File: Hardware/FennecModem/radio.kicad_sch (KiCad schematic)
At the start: 12 parts, among them J201 Conn_Coaxial, U201 DRA818V

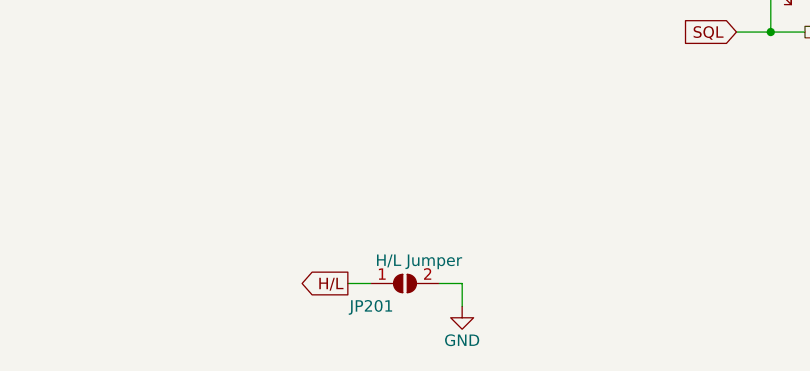
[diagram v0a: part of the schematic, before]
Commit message: Bump upstream libs with new logo
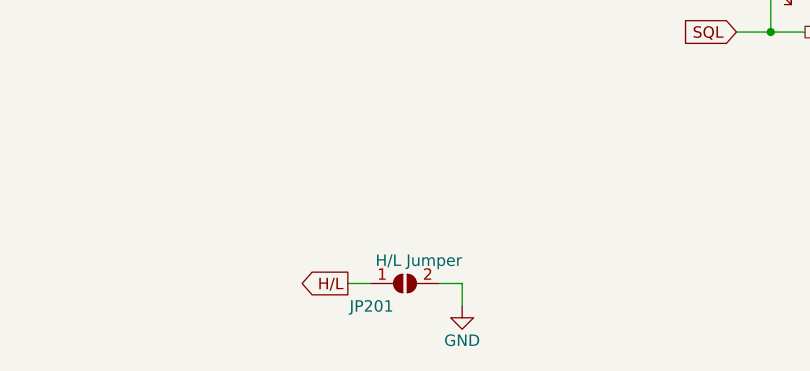
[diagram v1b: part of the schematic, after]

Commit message: Bump all pcb
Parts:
- removed JP201: H/L Jumper, Connector_PinHeader_2.54mm:PinHeader_1x02_P2.54mm_Vertical, symbol Jumper:SolderJumper_2_Open
- added D203: TX, LED_SMD:LED_0805_2012Metric, symbol Device:LED
- added D204: TXD, LED_SMD:LED_0805_2012Metric, symbol Device:LED
- added R205: 300, Resistor_SMD:R_0805_2012Metric, symbol Device:R
- added R206: 47R, Resistor_SMD:R_0805_2012Metric, symbol Device:R
- D201: footprint LED_SMD:LED_0603_1608Metric -> LED_SMD:LED_0805_2012Metric
- D202: value TX -> RXD; footprint LED_SMD:LED_0603_1608Metric -> LED_SMD:LED_0805_2012Metric
- R204: value 47R -> 300
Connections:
- net +5V: now also R203.2, R204.2, R205.2; no longer R203.1
- net PTT: now also D203.1 (K), R206.1; no longer D202.1 (K), R204.1, R204.2, U201.5 (PTT)
- net RXD: now also D202.1 (K)
- net TXD: now also D204.1 (K)
- net Sleep: now reaches R201.1, U201.6 (PD)
- net at D202.2 (A): now also R203.1; no longer R203.2
- new net: D203.2 (A), R205.1
- new net: D204.2 (A), R204.1
- new net: R206.2, U201.5 (PTT)
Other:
- note added: "LOW = Sleep HIGH = Normal"
- note added: "Pulldown = 0.5w Float = 1w"
- moved on the sheet: D201, R202

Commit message: Bump modem
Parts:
- D201, D203: footprint LED_SMD:LED_0805_2012Metric -> LED_THT:LED_D3.0mm_Horizontal_O1.27mm_Z2.0mm
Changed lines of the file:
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@@
       (effects (font (size 1.27 1.27)) (justify right))
     )
-    (property "Footprint" "LED_SMD:LED_0805_2012Metric" (at 205.105 155.575 0)
+    (property "Footprint" "LED_THT:LED_D3.0mm_Horizontal_O1.27mm_Z2.0mm" (at 205.105 155.575 0)
       (effects (font (size 1.27 1.27)) hide)
     )
@@
       (effects (font (size 1.27 1.27)) (justify right))
     )
-    (property "Footprint" "LED_SMD:LED_0805_2012Metric" (at 186.69 155.575 0)
-      (effects (font (size 1.27 1.27)) hide)
-    )
+    (property "Footprint" "LED_THT:LED_D3.0mm_Horizontal_O1.27mm_Z2.0mm" (at 186.69 155.575 0)
+      (effects (font (size 1.27 1.27)) hide)
+    )
